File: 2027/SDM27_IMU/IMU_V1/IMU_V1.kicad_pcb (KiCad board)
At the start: 4 copper layers, 42.5 x 32 mm, 80 parts, among them IC3 ISM330DHCXTR, IC7 IIS2MDCTR, J1 WEIPU SA12 7PIN, J3 USB_C_Receptacle_USB2.0_16P, SW1 SW_Push, SW2 SW_Push, U2 ESP32-C5HR8, U3 TPS2121RUXR, U4 TPS62901RPJR, U5 GD25Q32ESIG, U6 TLP175A_TPL,E, U7 USBLC6-2SC6, U8 TCAN3403DRBRQ1, Y3 CX1612DB48000D0FPJC1

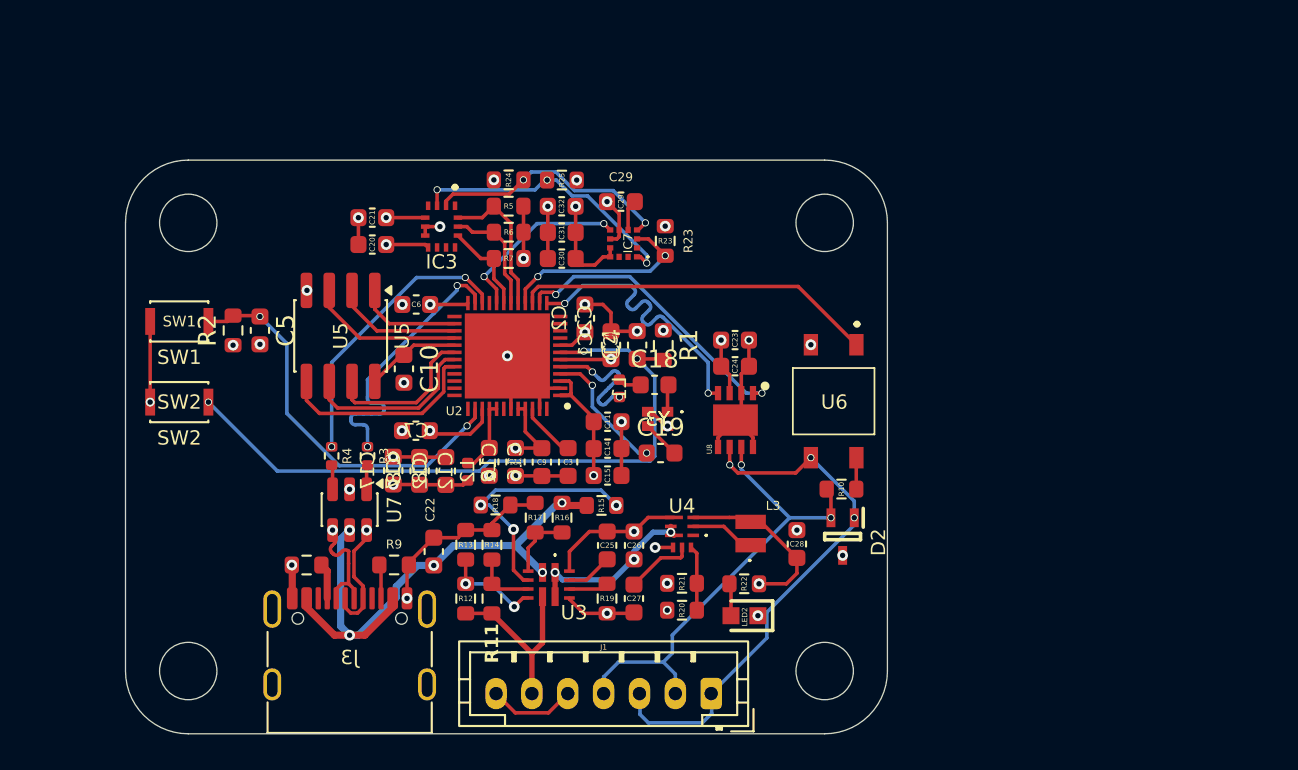
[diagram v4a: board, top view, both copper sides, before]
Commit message: IMU port
Just updating files for Laptop, silkscreen cleared up just needs stitching
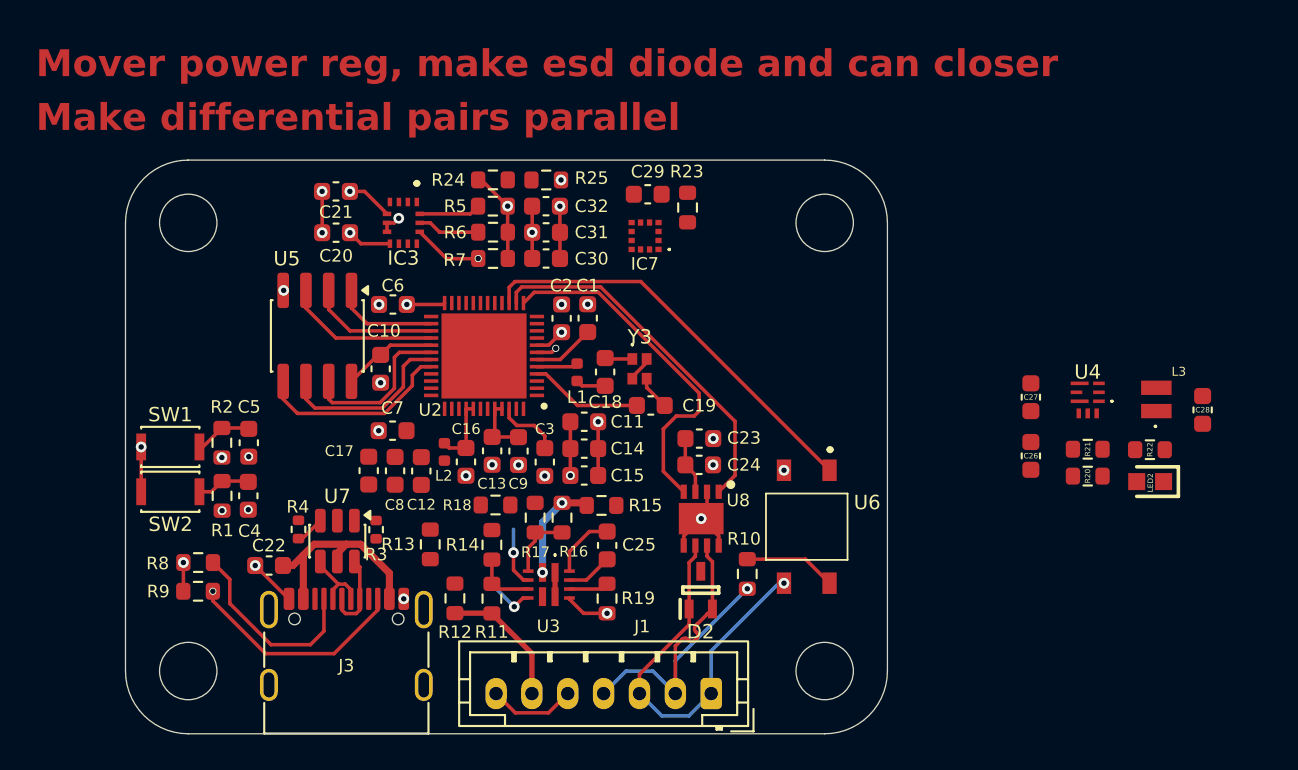
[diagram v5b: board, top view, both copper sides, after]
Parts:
- moved R1 26.0 mm to (119.4, 103.2), turned to 90 degrees
- moved C27 24.8 mm to (164.5, 97.7)
- moved U4 23.8 mm to (167.7, 97.7)
- moved LED2 23.8 mm to (171.2, 102.4)
- moved R20 23.8 mm to (167.7, 102.1)
- moved R21 23.8 mm to (167.7, 100.6)
- moved L3 23.8 mm to (171.5, 97.8)
- moved R22 23.8 mm to (171.1, 100.7)
- moved C28 23.8 mm to (174.1, 98.4)
- moved C4 23.3 mm to (120.9, 103.2), turned to -90 degrees
- moved C26 22.7 mm to (164.5, 101.0)
- moved R9 11.0 mm to (118.0, 108.6), turned to 180 degrees
- moved C22 9.22 mm to (122.0, 107.1), turned to 0 degrees
- moved D2 8.46 mm to (146.1, 108.5), turned to 90 degrees
- moved U6 7.16 mm to (152.0, 105.0)
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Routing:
- net GND: track 71.9 -> 34.3 mm, vias 30 -> 26
- net /CP: track 38.7 -> 4.07 mm, vias 3 -> 1
- net +3.3V: track 53.2 -> 30.2 mm, vias 19 -> 10
- net /BOOT: track 22.4 -> 2.95 mm, vias 2 -> 0
- net Net-(U2-GPIO13): track 15.9 -> 0.00 mm, vias 2 -> 0
- net Net-(U2-GPIO14): track 15.8 -> 0.00 mm, vias 2 -> 0
- net /SCX: track 15.7 -> 0.00 mm, vias 3 -> 0
- net VBUS: track 32.2 -> 17.9 mm, vias 5 -> 2
- net /SDX: track 13.9 -> 0.00 mm, vias 2 -> 0
- net /M_CS: track 11.3 -> 0.00 mm, vias 2 -> 0
- net Net-(J3-CC2): track 1.90 -> 12.6 mm, vias 0 -> 1
- net Net-(U3-OV2): track 14.0 -> 3.32 mm, vias 3 -> 1
- net /INT: track 10.2 -> 0.00 mm, vias 2 -> 0
- net Net-(J3-CC1): track 1.99 -> 11.0 mm
- net VCC: track 9.91 -> 1.35 mm, vias 3 -> 0
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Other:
- board text added: "Make differential pairs parallel"
- board text added: "Mover power reg, make esd diode and can closer"

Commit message: IMU V1 Finalized
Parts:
- moved R20 22.9 mm to (148.0, 90.5), turned to 180 degrees
- moved L3 22.5 mm to (149.2, 95.1), turned to -90 degrees
- moved C28 22.4 mm to (152.0, 94.5), turned to -90 degrees
- moved R21 21.4 mm to (148.0, 92.2), turned to 0 degrees
- moved R22 18.7 mm to (153.5, 94.5), turned to -90 degrees
- moved LED2 17.5 mm to (155.3, 95.0), turned to -90 degrees
- moved U4 16.6 mm to (151.1, 98.9), turned to -90 degrees
- moved C26 9.80 mm to (154.8, 100.0), turned to 0 degrees
- moved C27 9.78 mm to (154.8, 98.5), turned to 0 degrees
- moved R9 9.39 mm to (124.5, 101.7), turned to 90 degrees
- moved R8 7.22 mm to (123.0, 101.7), turned to 90 degrees
- moved C18 3.23 mm to (143.0, 94.0), turned to 0 degrees
- moved R23 1.22 mm to (145.6, 88.3)
- moved L1 0.32 mm to (138.9, 96.2), turned to 0 degrees
- moved C21 0.26 mm to (125.8, 86.5)
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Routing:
- net +3.3V: track 30.2 -> 59.9 mm, vias 10 -> 18
- net VCC: track 1.35 -> 27.6 mm, vias 0 -> 2
- net /SCX: track 0.00 -> 20.6 mm, vias 0 -> 3
- net /CP: track 4.07 -> 24.3 mm, vias 1 -> 2
- net GND: track 34.3 -> 54.4 mm, vias 26 -> 202
- net Net-(U2-GPIO13): track 0.00 -> 19.0 mm, vias 0 -> 2
- net Net-(U2-GPIO14): track 0.00 -> 18.9 mm, vias 0 -> 2
- net /SDX: track 0.00 -> 16.4 mm, vias 0 -> 3
- net /M_CS: track 0.00 -> 14.7 mm, vias 0 -> 2
- net /BOOT: track 2.95 -> 17.2 mm, vias 0 -> 2
- net /INT: track 0.00 -> 12.1 mm, vias 0 -> 2
- net Net-(U3-OV2): track 3.32 -> 13.8 mm, vias 1 -> 3
- net Net-(U4-VSET): track 0.00 -> 10.3 mm, vias 0 -> 2
- net VBUS: track 17.9 -> 26.6 mm, vias 2 -> 3
- net /I2C1_SDA: track 3.43 -> 9.23 mm
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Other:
- board text removed: "Make differential pairs parallel"
- board text removed: "Mover power reg, make esd diode and can closer"

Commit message: Library maintenance
edited some 3dmodles to point to their footprints. edited symbols and footprints to link properly. edited footprint and symbol library names in all projects 2026-2027 to use the same library nick name "SDM" for both  symbol and footprint.
all users must delete their old lib and make a new one named SDM for symbol and footprint.
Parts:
- LED2: footprint SDM Footprints:LEDC1608X80N -> SDM:LEDC1608X80N
- U3: footprint SDM Footprints:TPS2121RUXR -> SDM:TPS2121RUXR
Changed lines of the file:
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@@
 		)
 		(embedded_fonts no)
-		(model "TPS62901RPJR.stp"
+		(model "${SDM_MISC_3D}/TPS62901RPJR.stp"
 			(offset
 				(xyz 0 0 0)
@@
 		)
 		(embedded_fonts no)
-		(model "CX1612DB48000D0FPJC1.stp"
+		(model "${SDM_MISC_3D}/CX1612DB48000D0FPJC1.stp"
 			(offset
 				(xyz 0 0 0)
@@
 		)
 		(embedded_fonts no)
-		(model "TCAN3403DRBRQ1.stp"
+		(model "${SDM_MISC_3D}/TCAN3403DRBRQ1.stp"
 			(offset
 				(xyz 0 0 0)
@@
 		(embedded_fonts no)
 	)
-	(footprint "SDM Footprints:TPS2121RUXR"
+	(footprint "SDM:TPS2121RUXR"
 		(layer "F.Cu")
 		(at 137.611569 108.175903 -90)
@@
 		)
 		(embedded_fonts no)
-		(model "C:/Users/lazee/OneDrive/Documents/pcb-dev/MiscLibraries/SDM_Misc3D/TPS2121RUXR.stp"
+		(model "${SDM_MISC_3D}/TPS2121RUXR.stp"
 			(offset
 				(xyz 0 0 0)
@@
 		)
 	)
-	(footprint "SDM Footprints:LEDC1608X80N"
+	(footprint "SDM:LEDC1608X80N"
 		(layer "F.Cu")
 		(at 155.261867 94.995225 -90)
@@
 		)
 		(embedded_fonts no)
-		(model "${SDM_MISC3D}/ESP32-C5HR8.stp"
+		(model "${SDM_MISC_3D}/ESP32-C5HR8.stp"
 			(offset
 				(xyz 0 0 0)
@@
 		)
 		(embedded_fonts no)
-		(model "${SDM_MISC3D}/ISM330DHCXTR.step"
+		(model "${SDM_MISC_3D}/ISM330DHCXTR.step"
 			(offset
 				(xyz 0 0 0.86)
@@
 		)
 		(embedded_fonts no)
-		(model "F1C1-201612-2R2M.stp"
+		(model "${SDM_MISC_3D}/F1C1-201612-2R2M.stp"
 			(offset
 				(xyz -0.1899999948 -0.9100000126 0.05999999776)

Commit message: IMU Final Touches and Gerber/Drill Files
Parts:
- added G***: LOGO, LOGO, F.Cu at (118.5, 95.0)
- added G***: LOGO, LOGO, B.Cu at (130.0, 87.0)
- added G***: LOGO, LOGO, B.Cu at (136.0, 98.3)
- LED2: footprint SDM:LEDC1608X80N -> SDM Footprints:LEDC1608X80N
- U3: footprint SDM:TPS2121RUXR -> SDM Footprints:TPS2121RUXR
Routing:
- net GND: track 54.4 -> 77.4 mm, vias 202 -> 187
- net /CAN+: track 22.4 -> 17.3 mm, vias 1 -> 0
- net VCC: track 27.6 -> 28.6 mm
- net /CAN-: track 22.9 -> 23.1 mm, vias 1 -> 0
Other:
- board text added: "IMU V1"
